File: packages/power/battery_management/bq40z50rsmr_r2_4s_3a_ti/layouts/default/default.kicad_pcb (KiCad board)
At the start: 2 copper layers, 29 parts

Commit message: Make package builds deterministic by wiring explicit local parts
The remaining packages now reference package-local concrete passives,
inductors, and other small parts directly instead of relying on generic
part-picker resolution. This aligns the source with the local
assets and removes the flaky live EasyEDA lookup path that was blocking
verification.

Constraint: Builds must not depend on unstable live part-picking when local package assets already exist
Constraint: Package-local parts remain the ownership boundary; no shared global part store was introduced
Rejected: Keep generic passives as the default style | repeated verification failures from upstream EasyEDA API instability
Rejected: Add ad hoc offline hacks around ato part-picking | weaker than making the package source deterministic
Confidence: high
Scope-risk: moderate
Reversibility: clean
Directive: For packages that already own generated local parts, instantiate those part modules directly and avoid generic passive declarations unless there is a strong reason not to
Tested:  passed for stm32g0b1kbu6_st, mcp2518fdt_e_sl_microchip, tcan3413ddfr_ti, raspberry_pi_hat_socket_zhouri, bq40z50rsmr_r2_4s_3a_ti, tps56637rpar_5v1_5a_ti, tps62933drlr_3v3_ti, bq25756rrvr_4s_2a_ti, tps2121ruxr_20v_4a_ti, and tps25730drefr_20v_3a_ti
Not-tested: Cross-package downstream integration beyond each package's default/example build
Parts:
- C1, C2, C3, C4, C5, C6, C7, C9: value 100nF ±10% -> (none)
- C8: value 2.2µF ±10% -> (none)
- R1, R3, R5: value 100kΩ ±1% -> (none)
- R10, R11, R12, R13, R18, R2, R4, R8, R9: value 100Ω ±1% -> (none)
- R14, R15, R16, R17, R6: value 10kΩ ±1% -> (none)
- R7: value 1mΩ ±1% -> (none)
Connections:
- net 10 renamed 1-3
- net 11 renamed 1-4
- net 12 renamed 1-5
- net 13 renamed 1-6
- net 4 renamed 1-1
- net current_sense_filter-power-hv renamed srp_filtered
- net current_sense_filter-power-lv renamed srn_filtered
- net pack_bypass-power-hv renamed pack_filtered
- net pbi_hold_cap-power-hv renamed 1-2
- net vc1_filter_cap-power-hv renamed 1-9
- net vc2_filter_cap-power-hv renamed 1-8
- net vc2_filter_cap-power-lv renamed tap_1
- net vc3_filter_cap-power-hv renamed 1-7
- net vc3_filter_cap-power-lv renamed tap_2
- net vc4_filter_cap-power-hv renamed 2-2
- net vc4_filter_cap-power-lv renamed tap_3
- net vcc_bypass-power-hv renamed vcc_filtered
- C1 pad 1: hv -> 1
- C1 pad 2: lv -> 2
- C3 pad 2: lv -> 2
- C4 pad 2: lv -> 2
- C8 pad 2: lv -> 2
- C9 pad 2: lv -> 2
- Q1 pad 1: hv -> 1
- Q1 pad 2: 2 -> 2-1
- Q1 pad 3: pack-hv -> hv
- R1 pad 2: pack-hv -> hv
- R13 pad 1: hv -> 1
- R14 pad 2: lv -> 2
- R15 pad 2: lv -> 2
- R16 pad 2: lv -> 2
- R17 pad 2: lv -> 2
- R18 pad 1: hv -> 1
- R3 pad 1: 2 -> 2-1
- R3 pad 2: hv -> 1
- R4 pad 2: 2 -> 2-1
- R5 pad 1: hv -> 1
- R6 pad 1: pack-hv -> hv
- R7 pad 1: lv -> 2
- R7 pad 2: pack-lv -> lv
- R8 pad 1: lv -> 2
- R9 pad 1: pack-lv -> lv
- U1 pad 16: lv -> 2
- U1 pad 23: lv -> 2
- U1 pad 24: lv -> 2
- U1 pad 25: lv -> 2
- U1 pad 32: hv -> 1
- U1 pad 33: lv -> 2
- U1 pad 9: lv -> 2

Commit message: Make package schematics more readable and align passive choices with repo guidance
This pass improves the human-facing quality of the package library.
Explicit local capacitor/resistor parts now carry short descriptive
comments at the point of use, the MCP2518FD package swaps its 1uF bulk
capacitor to a 0603 part to match the current sizing rule, and several
packages add better net-name overrides for exposed and important internal
signals.

Constraint: Repo guidance now prefers explicit local parts and expects readable schematic net names
Constraint: Passive sizing should follow the current MLCC package rule unless a justified exception is needed
Rejected: Keep part instances comment-free | explicit local part names are not readable enough by themselves
Rejected: Leave the MCP2518FD 1uF bulk cap in 0402 | conflicts with the current 1uF-10uF 0603 guidance
Confidence: medium
Scope-risk: moderate
Reversibility: clean
Directive: When instantiating explicit local resistor/capacitor parts, include a short readable comment with the key value/package characteristics unless the name is already obviously human-readable
Tested:  passed for stm32g0b1kbu6_st, mcp2518fdt_e_sl_microchip, tcan3413ddfr_ti, raspberry_pi_hat_socket_zhouri, bq40z50rsmr_r2_4s_3a_ti, tps56637rpar_5v1_5a_ti, tps62933drlr_3v3_ti, bq25756rrvr_4s_2a_ti, tps2121ruxr_20v_4a_ti, and tps25730drefr_20v_3a_ti
Not-tested: Complete elimination of all internal autogenerated net labels in every package; some deep internal nets may still remain tool-driven
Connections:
- net 1 renamed CELL4
- net 1-1 renamed CHG_GATE
- net 1-2 renamed PBI_HOLD
- net 1-3 renamed TS1_BIAS
- net 1-4 renamed TS2_BIAS
- net 1-5 renamed TS3_BIAS
- net 1-6 renamed TS4_BIAS
- net 1-7 renamed VC3_FILT
- net 1-8 renamed VC2_FILT
- net 1-9 renamed VC1_FILT
- net 2 renamed GND
- net 2-1 renamed DSG_GATE
- net 2-2 renamed VC4_FILT
- net fet_common renamed FET_COMMON
- net hv renamed PACK+
- net pack_filtered renamed PACK_FILT
- net srn_filtered renamed SRN_FILT
- net srp_filtered renamed SRP_FILT
- net tap_1 renamed CELL1
- net tap_2 renamed CELL2
- net tap_3 renamed CELL3
- net vcc_filtered renamed BAT_FILT

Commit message: Expose raw battery connections without forcing net overrides
The battery frontend no longer assigns override_net_name values, and it now
exports raw_battery alongside the protected pack so downstream designs can add
a connector or harness wiring at the package boundary. I also removed the
repository guidance that encouraged override-based naming and rebuilt the
checked-in layouts so their net metadata matches the source after the change.

Constraint: Package instances were breaking when internal net overrides propagated into downstream designs
Constraint: The protected pack API and 4S/3A electrical limits must remain intact
Rejected: Keep pack-only exposure and require downstream forks | blocks connector integration at the package boundary
Rejected: Leave checked-in layouts on the old net names | creates source/layout drift after rebuilds
Confidence: high
Scope-risk: moderate
Reversibility: clean
Directive: Prefer explicit exported interfaces like `pack` and `raw_battery` over internal net-name overrides
Tested: `uv tool run --from atopile==0.15.4 ato --non-interactive build` in `packages/power/battery_management/bq40z50rsmr_r2_4s_3a_ti`
Not-tested: Integration of `raw_battery` with a concrete downstream battery connector package
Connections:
- net BAT_FILT renamed vcc_filtered
- net CELL1 renamed tap_1
- net CELL2 renamed tap_2
- net CELL3 renamed tap_3
- net CELL4 renamed hv
- net CHG_GATE renamed 1
- net DSG_GATE renamed 2
- net FET_COMMON renamed fet_common
- net PACK+ renamed pack-hv
- net PACK_FILT renamed pack_filtered
- net PBI_HOLD renamed 1-1
- net SRN_FILT renamed srn_filtered
- net SRP_FILT renamed srp_filtered
- net TS1_BIAS renamed 1-2
- net TS2_BIAS renamed 1-3
- net TS3_BIAS renamed 1-4
- net TS4_BIAS renamed 1-5
- net VC1_FILT renamed 1-8
- net VC2_FILT renamed 1-7
- net VC3_FILT renamed 1-6
- net VC4_FILT renamed 2-1
- C1 pad 2: GND -> lv
- C3 pad 2: GND -> lv
- C4 pad 2: GND -> lv
- C8 pad 2: GND -> lv
- C9 pad 2: GND -> lv
- R14 pad 2: GND -> lv
- R15 pad 2: GND -> lv
- R16 pad 2: GND -> lv
- R17 pad 2: GND -> lv
- R7 pad 1: GND -> lv
- R7 pad 2: lv -> pack-lv
- R8 pad 1: GND -> lv
- R9 pad 1: lv -> pack-lv
- U1 pad 16: GND -> lv
- U1 pad 23: GND -> lv
- U1 pad 24: GND -> lv
- U1 pad 25: GND -> lv
- U1 pad 33: GND -> lv
- U1 pad 9: GND -> lv

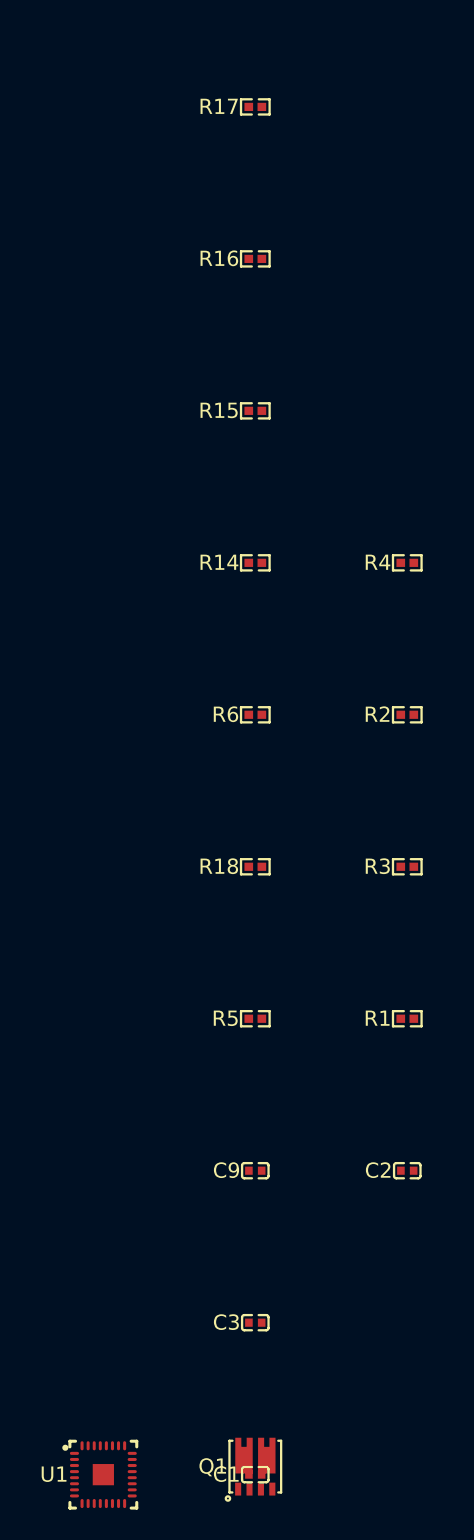
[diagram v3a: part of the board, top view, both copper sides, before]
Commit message: Align the BQ40Z50 frontend with TI's recommended sense filtering
The cell-tap, SMBus, unused-pin, and PTC wiring had drifted from the TI
reference guidance. This updates the package so VC filtering happens on the
IC side of the 100 Ω resistors, unused TS/DISP pins are grounded, SMBus gets
series damping, unnecessary bypass caps are removed, and the PTC safety path
uses a concrete 0402 Murata part.

Constraint: Must keep the package reusable, deterministic, and sourced from LCSC parts already compatible with Atopile
Constraint: Verification must use ato in the changed package directory
Rejected: Keep TS pull-down resistors for unused inputs | datasheet guidance prefers direct VSS ties in this case
Rejected: Leave PTC unimplemented | user explicitly requested a concrete safety thermistor path
Confidence: medium
Scope-risk: moderate
Reversibility: clean
Directive: Re-check BQ40Z50 data-flash temperature and permanent-fail settings before changing the chosen PTC trip part or threshold assumptions
Tested:  in packages/power/battery_management/bq40z50rsmr_r2_4s_3a_ti (default and example)
Not-tested: Bench-level thermal trip behavior and SMBus signal integrity on hardware
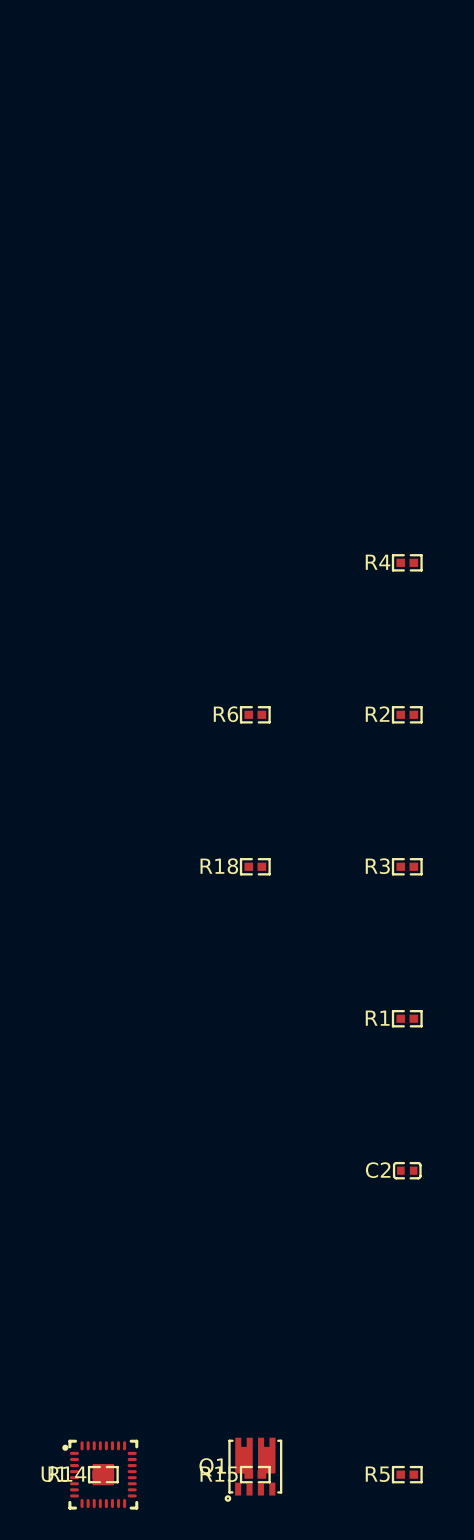
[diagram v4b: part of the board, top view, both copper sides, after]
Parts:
- removed C1, C3, C9: , Murata_Electronics_GRM155R71H104KE14D:C0402
- removed R16, R17: , YAGEO_RC0402FR_0710KL:R0402
- R14, R15: footprint YAGEO_RC0402FR_0710KL:R0402 -> YAGEO_RC0402FR_07100RL:R0402
- R5: footprint YAGEO_RC0402FR_07100KL:R0402 -> Murata_Electronics_PRF15BB103RB6RC:R0402
- moved R15 70.0 mm to (10.0, 0.00)
- moved R14 60.8 mm to (0.00, 0.00)
- moved R5 31.6 mm to (20.0, 0.00)
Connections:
- net 2-1 renamed vc4_filtered
- C4 pad 1: 1-8 -> vc1_filtered
- C4 pad 2: lv -> raw_battery-lv
- C5 pad 1: 1-7 -> vc2_filtered
- C5 pad 2: tap_1 -> vc1_filtered
- C6 pad 1: 1-6 -> vc3_filtered
- C6 pad 2: tap_2 -> vc2_filtered
- C7 pad 2: tap_3 -> vc3_filtered
- C8 pad 2: lv -> raw_battery-lv
- Q1 pad 1: hv -> raw_battery-hv
- Q1 pad 3: pack-hv -> hv
- R1 pad 2: pack-hv -> hv
- R10 pad 2: 1-8 -> vc1_filtered
- R11 pad 2: 1-7 -> vc2_filtered
- R12 pad 2: 1-6 -> vc3_filtered
- R13 pad 1: hv -> raw_battery-hv
- R14 pad 1: 1-2 -> SCL
- R14 pad 2: lv -> SMBC
- R15 pad 1: 1-3 -> SDA
- R15 pad 2: lv -> SMBD
- R18 pad 1: hv -> raw_battery-hv
- R3 pad 2: hv -> raw_battery-hv
- R5 pad 1: hv -> PTC
- R5 pad 2: nDISP -> raw_battery-hv
- R6 pad 1: pack-hv -> hv
- R7 pad 1: lv -> raw_battery-lv
- R7 pad 2: pack-lv -> lv
- R8 pad 1: lv -> raw_battery-lv
- R9 pad 1: pack-lv -> lv
- U1 pad 10: 1-2 -> raw_battery-lv
- U1 pad 11: 1-3 -> raw_battery-lv
- U1 pad 12: 1-4 -> raw_battery-lv
- U1 pad 13: 1-5 -> raw_battery-lv
- U1 pad 16: lv -> raw_battery-lv
- U1 pad 17: nDISP -> raw_battery-lv
- U1 pad 18: SDA -> SMBD
- U1 pad 19: SCL -> SMBC
- U1 pad 23: lv -> PTC
- U1 pad 24: lv -> raw_battery-hv
- U1 pad 25: lv -> raw_battery-lv
- U1 pad 3: 1-6 -> vc3_filtered
- U1 pad 32: hv -> raw_battery-hv
- U1 pad 33: lv -> raw_battery-lv
- U1 pad 4: 1-7 -> vc2_filtered
- U1 pad 5: 1-8 -> vc1_filtered
- U1 pad 9: lv -> raw_battery-lv

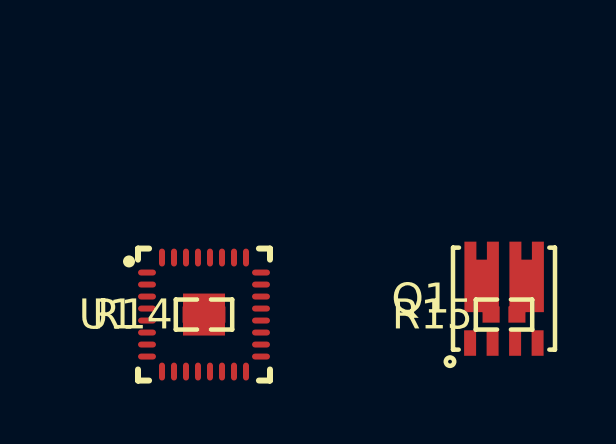
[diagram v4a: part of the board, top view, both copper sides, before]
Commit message: Filter the BQ40Z50 PTC input against switching noise
The new FET safety PTC path benefits from a local filter capacitor so the gauge
sees a cleaner temperature-protection signal instead of raw switching noise from
the pack side. This adds the requested 100 nF capacitor from PTC to BAT using
an existing package-local Murata MLCC.

Constraint: Must preserve the existing deterministic package-local part set where possible
Constraint: Verification must be done with ato in the changed package directory
Rejected: Add a new capacitor value/package just for the PTC node | existing 100 nF 0402 Murata part already fits the request
Rejected: Leave the PTC input unfiltered | user explicitly requested a filter capacitor
Confidence: high
Scope-risk: narrow
Reversibility: clean
Directive: Keep the PTC filter referenced to BAT unless the underlying TI protection network is re-derived from datasheet guidance
Tested:  in packages/power/battery_management/bq40z50rsmr_r2_4s_3a_ti (default and example)
Not-tested: Hardware-level noise immunity and trip response around the PTC input
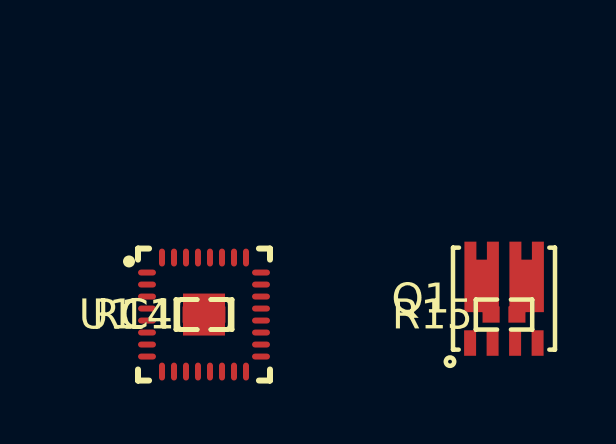
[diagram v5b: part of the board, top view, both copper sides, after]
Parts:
- added C1: , Murata_Electronics_GRM155R71E104KE14D:C0402, F.Cu at (0.00, 0.00)
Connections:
- C8 pad 1: 1-1 -> 1-2
- R5 pad 1: PTC -> 1-1
- U1 pad 1: 1-1 -> 1-2
- U1 pad 23: PTC -> 1-1
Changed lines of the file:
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@@
 	(net 29 "CHG")
 	(net 30 "srp_filtered")
-	(net 32 "1-1")
+	(net 32 "1-2")
 	(net 35 "BTP_INT")
 	(net 38 "LEDCNTLA")
@@
 	(net 2 "raw_battery-lv")
 	(net 4 "SMBD")
-	(net 5 "PTC")
 	(net 6 "raw_battery-hv")
 	(net 7 "SCL")
@@
 	(net 11 "vc3_filtered")
 	(net 12 "vc2_filtered")
+	(net 1 "1-1")
 	(footprint "XNRUSEMI_XRS30V06D:DFN-8_L3.3-W3.3-P0.75-TL"
 		(layer "F.Cu")
@@
 			(size 0.6 0.2)
 			(layers "F.Cu" "F.Paste" "F.Mask")
-			(net 5 "PTC")
+			(net 1 "1-1")
 		)
 		(pad "22" smd oval
@@
 			(size 0.6 0.2)
 			(layers "F.Cu" "F.Paste" "F.Mask")
-			(net 32 "1-1")
+			(net 32 "1-2")
 		)
 		(pad "33" smd rect
@@
 			(size 0.8 0.9)
 			(layers "F.Cu" "F.Paste" "F.Mask")
-			(net 32 "1-1")
+			(net 32 "1-2")
 		)
 		(embedded_fonts no)
@@
 			(size 0.57 0.54)
 			(layers "F.Cu" "F.Paste" "F.Mask")
-			(net 5 "PTC")
+			(net 1 "1-1")
 		)
 		(embedded_fonts no)
@@
 			(offset
 				(xyz 0 0 -0)
+			)
+			(scale
+				(xyz 1 1 1)
+			)
+			(rotate
+				(xyz 0 0 0)
+			)
+		)
+	)
+	(footprint "Murata_Electronics_GRM155R71E104KE14D:C0402"
+		(layer "F.Cu")
+		(at 0 0 0)
+		(property "Reference" "C1"
+			(at -0.97 0 0)
+			(layer "F.SilkS")
+			(effects
+				(font
+					(size 1 1)
+					(thickness 0.15)
+				)
+				(justify right)
+			)
+		)
+		(property "Value" ""
+			(at 0 4)
+			(layer "F.Fab")
+			(effects
+				(font
+					(size 1 1)
+					(thickness 0.15)
+				)
+			)
+		)
+		(property "LCSC" "C77014"
+			(at 0 0 0)
+			(layer "User.9")
+			(hide yes)
+		)
+		(property "Manufacturer" "Murata Electronics"
+			(at 0 0 0)
+			(layer "User.9")
+			(hide yes)
+		)
+		(property "Partnumber" "GRM155R71E104KE14D"
+			(at 0 0 0)
+			(layer "User.9")
+			(hide yes)
+		)
+		(property "Datasheet" "https://www.lcsc.com/datasheet/lcsc_datasheet_1811081616_Murata-Electronics-GRM155R71E104KE14D_C77014.pdf"
+			(at 0 0 0)
+			(layer "User.9")
+			(hide yes)
+		)
+		(property "atopile_address" "fet_safety_ptc_filter"
+			(at 0 0 0)
+			(layer "User.9")
+			(hide yes)
+		)
+		(property "lcsc_id" "C77014"
+			(at 0 0 0)
+			(layer "User.9")
+			(hide yes)
+		)
+		(attr smd)
+		(fp_line
+			(start -0.72 -0.5)
+			(end -0.22 -0.5)
+			(stroke
+				(width 0.15)
+				(type solid)
+			)
+			(layer "F.SilkS")
+			(layers "F.SilkS")
+			(locked no)
+		)
+		(fp_line
+			(start -0.87 0.35)
+			(end -0.87 -0.35)
+			(stroke
+				(width 0.15)
+				(type solid)
+			)
+			(layer "F.SilkS")
+			(layers "F.SilkS")
+			(locked no)
+		)
+		(fp_line
+			(start -0.22 0.5)
+			(end -0.72 0.5)
+			(stroke
+				(width 0.15)
+				(type solid)
+			)
+			(layer "F.SilkS")
+			(layers "F.SilkS")
+			(locked no)
+		)
+		(fp_line
+			(start 0.72 0.5)
+			(end 0.22 0.5)
+			(stroke
+				(width 0.15)
+				(type solid)
+			)
+			(layer "F.SilkS")
+			(layers "F.SilkS")
+			(locked no)
+		)
+		(fp_line
+			(start 0.22 -0.5)
+			(end 0.72 -0.5)
+			(stroke
+				(width 0.15)
+				(type solid)
+			)
+			(layer "F.SilkS")
+			(layers "F.SilkS")
+			(locked no)
+		)
+		(fp_line
+			(start 0.87 -0.35)
+			(end 0.87 0.35)
+			(stroke
+				(width 0.15)
+				(type solid)
+			)
+			(layer "F.SilkS")
+			(layers "F.SilkS")
+			(locked no)
+		)
+		(fp_arc
+			(start 0.87 -0.35)
+			(mid 0.826066 -0.456066)
+			(end 0.72 -0.5)
+			(stroke
+				(width 0.15)
+				(type solid)
+			)
+			(layer "F.SilkS")
+			(locked no)
+		)
+		(fp_arc
+			(start 0.72 0.5)
+			(mid 0.826066 0.456066)
+			(end 0.87 0.35)
+			(stroke
+				(width 0.15)
+				(type solid)
+			)
+			(layer "F.SilkS")
+			(locked no)
+		)
+		(fp_arc
+			(start -0.87 0.35)
+			(mid -0.826066 0.456066)
+			(end -0.72 0.5)
+			(stroke
+				(width 0.15)
+				(type solid)
+			)
+			(layer "F.SilkS")
+			(locked no)
+		)
+		(fp_arc
+			(start -0.72 -0.5)
+			(mid -0.826066 -0.456066)
+			(end -0.87 -0.35)
+			(stroke
+				(width 0.15)
+				(type solid)
+			)
+			(layer "F.SilkS")
+			(locked no)
+		)
+		(fp_circle
+			(center -0.5 0.25)
+			(end -0.47 0.25)
+			(stroke
+				(width 0.06)
+				(type solid)
+			)
+			(layer "F.Fab")
+			(locked no)
+		)
+		(pad "2" smd rect
+			(at 0.42 0 0)
+			(size 0.5 0.54)
+			(layers "F.Cu" "F.Paste" "F.Mask")
+			(net 6 "raw_battery-hv")
+		)
+		(pad "1" smd rect
+			(at -0.42 0 0)
+			(size 0.5 0.54)
+			(layers "F.Cu" "F.Paste" "F.Mask")
+			(net 1 "1-1")
+		)
+		(embedded_fonts no)
+		(model "${KIPRJMOD}/../../parts/Murata_Electronics_GRM155R71E104KE14D/C0402_L1.0-W0.5-H0.5.step"
+			(offset
+				(xyz 0 0 -0)
